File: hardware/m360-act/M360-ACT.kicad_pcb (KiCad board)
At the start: 2 copper layers, 100 x 80 mm, 30 parts, among them J1 5V do quadro, J2 M360-RF, J3 RJ45 RELES-A, J4 RJ45 RELES-B, J5 RJ45 SENSORES, SW1 Repareamento, U1 AMS1117-3.3, U2 74HCT244, U3 CD74HC4067, U4 SRV05-4, U5 SRV05-4, U6 SRV05-4, U7 SRV05-4, U8 SRV05-4

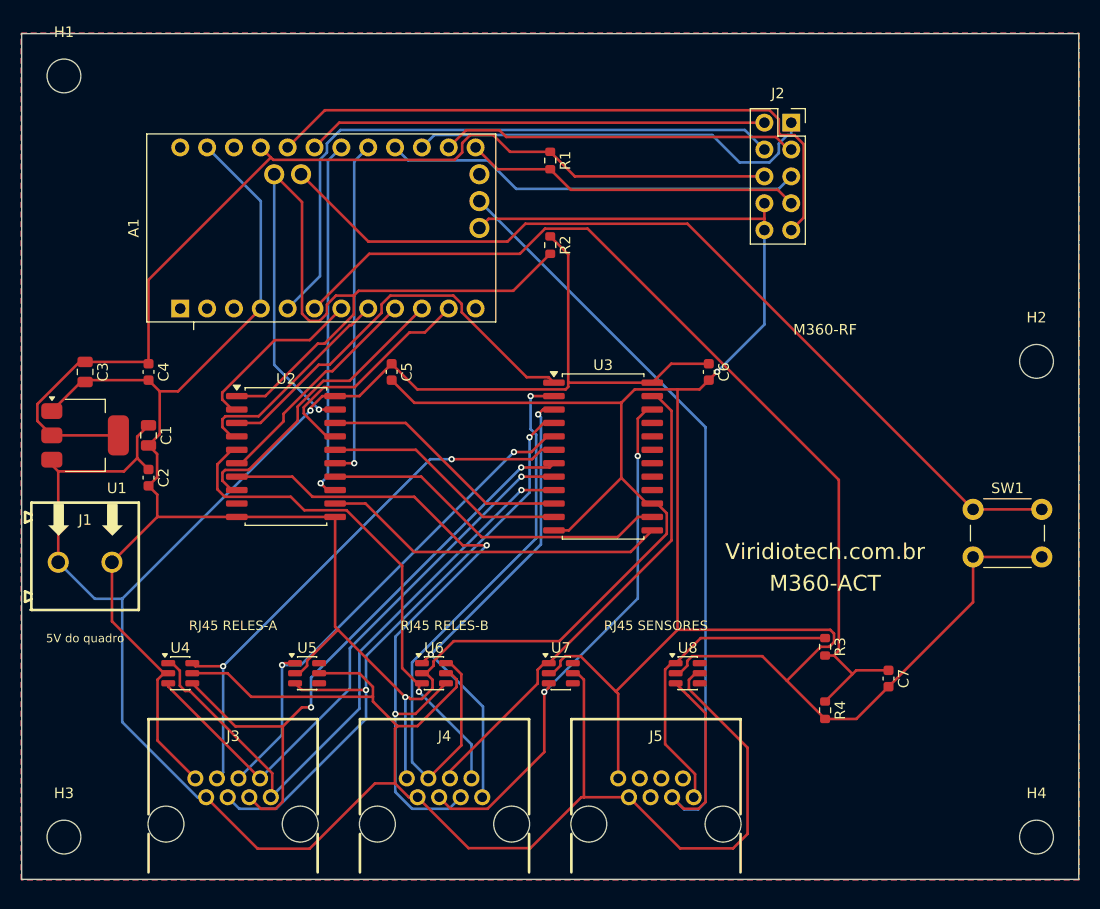
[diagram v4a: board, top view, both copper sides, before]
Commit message: feat(hardware): placa da M360-ACT refeita e arquivos de fabricação
- sincronizada com o esquemático (35 peças novas; U1 ME6211, SW1 reed)
- place_act.py reescrito: par de TVS a 180° atrás de cada RJ45, 100 ohm na
  ordem de saída dos TVS, U3 com I0-I7 para os TVS, reed na borda direita,
  fiduciais, área sem trilha em B.Cu sob os RJ45; borne J1 a rot 90 (entrada
  dos fios para a borda, datasheet C8465) e modelo 3D do borne corrigido
- roteamento pela §11.8: 15 pernas RJ45 -> TVS numa passada, em F.Cu;
  REL_CH0/CH6 desenhados à mão; tronco de +5V em 0,5 mm; classe Power
- ordem_tvs.py: contato por distância entre segmentos (pega X e sobreposição)
- silk_refs.py: referências posicionadas automaticamente
- correções da revisão adversarial da placa; reed: porta do quadro aberta
- fabricacao/: Gerbers, BOM e posição (53 peças, todas com LCSC)

DRC --severity-all 0/0, paridade idêntica, ordem_tvs act 15/15.

Co-Authored-By: Claude Opus 5 (1M context) <noreply@anthropic.com>
Claude-Session: https://claude.ai/code/session_012t7RkcrXvvpDVjKVimNu18
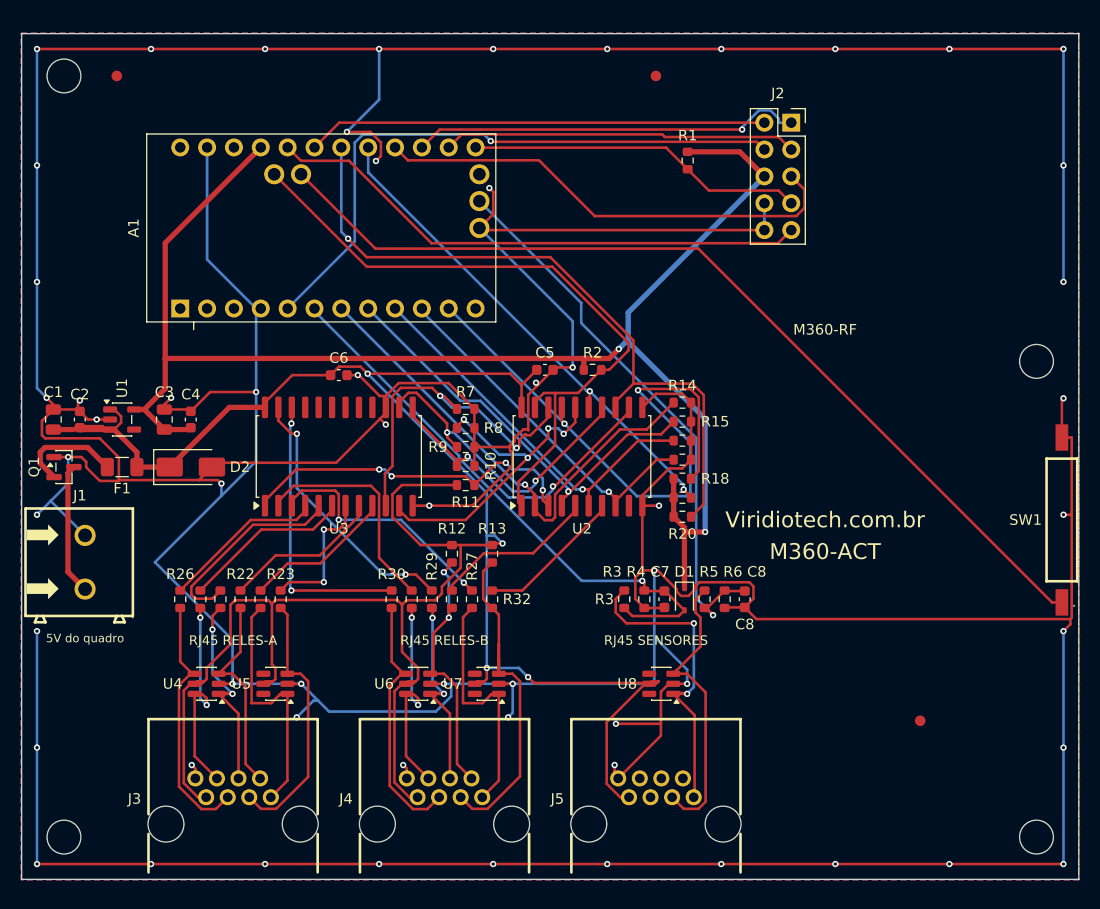
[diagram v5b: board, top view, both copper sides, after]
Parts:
- added C8: 100nF, Capacitor_SMD:C_0603_1608Metric, F.Cu at (168.4, 153.5)
- added D1: BAT54WS, Diode_SMD:D_SOD-323, F.Cu at (162.7, 153.5)
- added D2: SMAJ5.0A, Diode_SMD:D_SMA, F.Cu at (116.0, 141.0)
- added F1: 500mA, Fuse:Fuse_1206_3216Metric, F.Cu at (109.5, 141.0)
- added FID1: Fiducial_1mm_Mask2mm, Fiducial_1mm_Mask2mm, F.Cu at (109.0, 104.0)
- added FID2: Fiducial_1mm_Mask2mm, Fiducial_1mm_Mask2mm, F.Cu at (160.0, 104.0)
- added FID3: Fiducial_1mm_Mask2mm, Fiducial_1mm_Mask2mm, F.Cu at (185.0, 165.0)
- added Q1: AO3401A, Package_TO_SOT_SMD:SOT-23, F.Cu at (104.0, 141.0)
- added R10: 100k, Resistor_SMD:R_0603_1608Metric, F.Cu at (142.0, 140.9)
- added R11: 100k, Resistor_SMD:R_0603_1608Metric, F.Cu at (142.0, 142.7)
- added R12: 100k, Resistor_SMD:R_0603_1608Metric, F.Cu at (140.7, 149.2)
- added R13: 100k, Resistor_SMD:R_0603_1608Metric, F.Cu at (144.5, 149.2)
- added R14: 100k, Resistor_SMD:R_0603_1608Metric, F.Cu at (162.5, 134.9)
- added R15: 100k, Resistor_SMD:R_0603_1608Metric, F.Cu at (162.5, 136.7)
- added R16: 100k, Resistor_SMD:R_0603_1608Metric, F.Cu at (162.5, 138.5)
- added R17: 100k, Resistor_SMD:R_0603_1608Metric, F.Cu at (162.5, 140.3)
- added R18: 100k, Resistor_SMD:R_0603_1608Metric, F.Cu at (162.5, 142.1)
- added R19: 100k, Resistor_SMD:R_0603_1608Metric, F.Cu at (162.5, 143.9)
- added R20: 100k, Resistor_SMD:R_0603_1608Metric, F.Cu at (162.5, 145.7)
- added R21: 100, Resistor_SMD:R_0603_1608Metric, F.Cu at (122.6, 153.5)
- added R22: 100, Resistor_SMD:R_0603_1608Metric, F.Cu at (120.7, 153.5)
- added R23: 100, Resistor_SMD:R_0603_1608Metric, F.Cu at (124.5, 153.5)
- added R24: 100, Resistor_SMD:R_0603_1608Metric, F.Cu at (116.9, 153.5)
- added R25: 100, Resistor_SMD:R_0603_1608Metric, F.Cu at (118.8, 153.5)
- added R26: 100, Resistor_SMD:R_0603_1608Metric, F.Cu at (115.0, 153.5)
- added R27: 100, Resistor_SMD:R_0603_1608Metric, F.Cu at (142.6, 153.5)
- added R28: 100, Resistor_SMD:R_0603_1608Metric, F.Cu at (136.9, 153.5)
- added R29: 100, Resistor_SMD:R_0603_1608Metric, F.Cu at (138.8, 153.5)
- added R30: 100, Resistor_SMD:R_0603_1608Metric, F.Cu at (135.0, 153.5)
- added R31: 100, Resistor_SMD:R_0603_1608Metric, F.Cu at (140.7, 153.5)
- added R32: 100, Resistor_SMD:R_0603_1608Metric, F.Cu at (144.5, 153.5)
- added R5: 10k, Resistor_SMD:R_0603_1608Metric, F.Cu at (164.6, 153.5)
- added R6: 20k, Resistor_SMD:R_0603_1608Metric, F.Cu at (166.5, 153.5)
- added R7: 100k, Resistor_SMD:R_0603_1608Metric, F.Cu at (142.0, 135.5)
- added R8: 100k, Resistor_SMD:R_0603_1608Metric, F.Cu at (142.0, 137.3)
- added R9: 100k, Resistor_SMD:R_0603_1608Metric, F.Cu at (142.0, 139.1)
- SW1: value Repareamento -> Reed; footprint Button_Switch_THT:SW_PUSH_6mm -> M360:Reed_Littelfuse_59170
- U1: value AMS1117-3.3 -> ME6211C33M5; footprint Package_TO_SOT_SMD:SOT-223-3_TabPin2 -> Package_TO_SOT_SMD:SOT-23-5
- moved C6 35.0 mm to (130.0, 132.3), turned to 0 degrees
- moved U2 28.0 mm to (153.0, 140.0), turned to 90 degrees
- moved U3 25.0 mm to (130.0, 140.0), turned to 90 degrees
- moved C7 22.5 mm to (160.8, 153.5)
- moved R4 20.1 mm to (158.9, 153.5)
- moved R3 19.5 mm to (157.0, 153.5)
- moved C5 14.5 mm to (149.5, 131.8), turned to 0 degrees
- moved R1 13.0 mm to (163.0, 112.0)
- moved R2 12.5 mm to (154.0, 131.8), turned to 0 degrees
- moved C1 9.12 mm to (103.0, 136.5), turned to 90 degrees
- moved C3 8.75 mm to (113.5, 136.5), turned to 90 degrees
- moved C2 8.51 mm to (105.5, 136.5), turned to 90 degrees
- moved SW1 8.46 mm to (198.4, 146.0), turned to 90 degrees
- moved U7 7.07 mm to (144.0, 161.5), turned to 180 degrees
- moved C4 6.02 mm to (116.0, 136.5), turned to 90 degrees
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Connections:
- J1 pad 1: +5V -> VIN_RAW
- J5 pad 3: AUX_A6 -> AUX_A6_IN
- R2 pad 1: +5V -> 3V3
- U1 pad 1: GND -> +5V
- U1 pad 2: 3V3 -> GND
- U2 pad 5: REL_NFT -> REL_NFT_BUF
- U2 pad 7: REL_OXI -> REL_OXI_BUF
- U3 pad 2: REL_CH7 -> REL_CH7_MUX
- U3 pad 22: REL_CH9 -> REL_CH9_MUX
- U3 pad 23: REL_CH8 -> REL_CH8_MUX
- U3 pad 3: REL_CH6 -> REL_CH6_MUX
- U3 pad 4: REL_CH5 -> REL_CH5_MUX
- U3 pad 5: REL_CH4 -> REL_CH4_MUX
- U3 pad 6: REL_CH3 -> REL_CH3_MUX
- U3 pad 7: REL_CH2 -> REL_CH2_MUX
- U3 pad 8: REL_CH1 -> REL_CH1_MUX
- U3 pad 9: REL_CH0 -> REL_CH0_MUX
- U4 pad 1: REL_CH0 -> REL_CH4
- U4 pad 4: REL_CH2 -> REL_CH5
- U5 pad 1: REL_CH4 -> REL_CH0
- U5 pad 3: REL_CH5 -> REL_CH2
- U6 pad 1: REL_CH6 -> REL_CH8
- U6 pad 4: REL_OXI -> REL_CH9
- U7 pad 1: REL_CH8 -> REL_CH6
- U7 pad 3: REL_CH9 -> REL_OXI
- U8 pad 3: AUX_A6 -> AUX_A6_IN
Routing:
- net GND: track 387.8 -> 747.5 mm, vias 2 -> 59
- net 3V3: track 97.6 -> 145.2 mm, vias 0 -> 2
- net +5V: track 271.0 -> 230.6 mm, vias 1 -> 4
- net REL_CH7: track 57.1 -> 19.6 mm, vias 1 -> 2
- net REL_CH0: track 59.3 -> 22.8 mm, vias 1 -> 0
- net FLOW_DIV: track 89.9 -> 53.8 mm, vias 0 -> 1
- net MUX_SIG_3V3: track 22.0 -> 57.8 mm, vias 0 -> 2
- net REL_CH5: track 59.9 -> 24.2 mm, vias 2 -> 0
- net REL_CH1: track 54.5 -> 19.7 mm, vias 1 -> 0
- net REL_CH3: track 53.7 -> 19.6 mm
- net REL_CH2: track 58.9 -> 25.4 mm, vias 2 -> 0
- net AUX_A6: track 85.9 -> 53.7 mm, vias 0 -> 1
- net REL_OXI: track 66.5 -> 34.6 mm, vias 2 -> 0
- net OXI_3V3: track 34.2 -> 66.0 mm
- net MUX_S0_3V3: track 17.0 -> 46.5 mm, vias 0 -> 1
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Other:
- board text added: "R3 R4 C7 D1 R5 R6 C8"

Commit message: fix(hardware): ACT — placa de 93 mm e roteamento completado após ajustes do usuário
- ajustes do usuário: borda direita em x 193, soquete J2 a 90°, SW1, H2 e H4
  reposicionados, marca e legenda do J2 em pé; place_act.py e silk_act.py
  passam a reproduzi-los
- contorno fechado em 93 x 80 mm; zonas de GND estendidas até a nova borda
  (por texto); SPI, DIO, RF_RESET, REED e trechos de GND/3V3 rerroteados com
  o resto travado; costura do perímetro refeita
- §11.7: SetOutline de zona pelo SWIG + SaveBoard zerou o .kicad_pcb
- fabricacao/ regenerado (53 peças)

DRC --severity-all 0/0, paridade idêntica, ordem_tvs act 15/15.

Co-Authored-By: Claude Opus 5 (1M context) <noreply@anthropic.com>
Claude-Session: https://claude.ai/code/session_012t7RkcrXvvpDVjKVimNu18
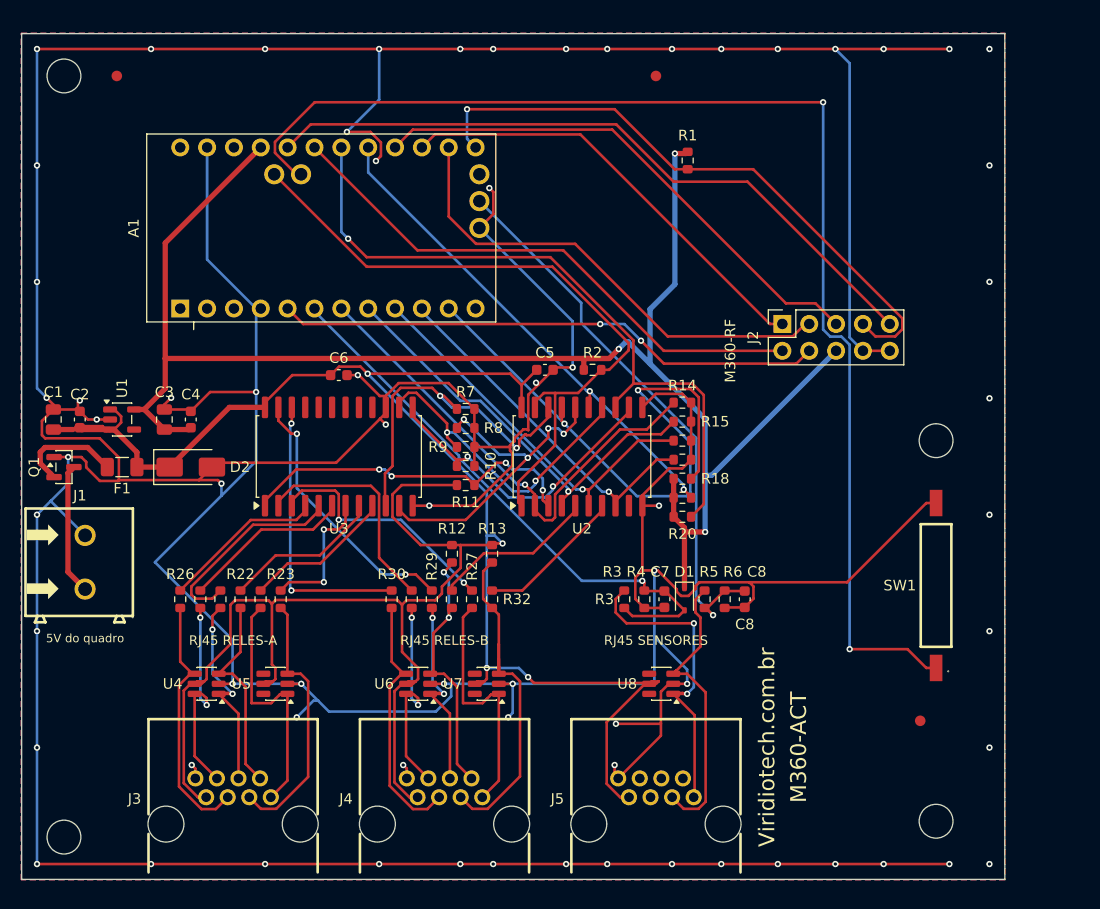
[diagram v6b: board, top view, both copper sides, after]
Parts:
- moved J2 19.1 mm to (172.0, 127.5), turned to 90 degrees
- moved SW1 13.4 mm to (186.5, 152.2)
- moved H2 12.1 mm to (186.5, 138.5)
- moved H4 9.62 mm to (186.5, 174.5)
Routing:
- net GND: track 747.5 -> 661.1 mm, vias 59 -> 69
- net REED: track 88.7 -> 120.1 mm, vias 0 -> 2
- net NSS: track 32.0 -> 58.8 mm, vias 0 -> 1
- net RF_RESET: track 51.9 -> 65.7 mm
- net MOSI: track 33.5 -> 45.8 mm
- net 3V3: track 145.2 -> 155.4 mm, vias 2 -> 3
- net DIO1: track 43.5 -> 52.2 mm
- net DIO0: track 58.0 -> 52.0 mm, vias 1 -> 2
- net MISO: track 37.2 -> 42.0 mm, vias 1 -> 0
- net SCK: track 45.2 -> 50.0 mm
- net REL_OXI: track 34.6 -> 35.3 mm
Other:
- board size 100 x 80 mm -> 93 x 80 mm

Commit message: feat(hardware): header 1x8 do nRF24 legado nas placas GW, LP e ACT
- esquemáticos: header 1x8 "nRF24 legado" (GW J4, LP J5, ACT J6; C492407,
  solda manual, fora do BOM e da posição) e 10 uF 0805 (C5/C16/C9, C15850)
  nas mesmas redes do soquete do mezanino: CE = DIO0, CSN = NSS, IRQ = DIO1
  (sem ligação na GW). Um rádio por placa: nRF24 OU mezanino RFM95W
- tools/add_nrf_header.py: grava símbolo, fios e labels por texto, embute o
  Conn_01x08 stock e confere colisão; netdiff só nas redes previstas, ERC 0,
  campos e lib_symbols inalterados nas três folhas
- placas rerroteadas sem apagar a fiação existente (DSN com fios fixos e
  cobertos por área proibida, mais áreas proibidas sobre os fiduciais);
  vias de GND junto do pino 8 e do capacitor; legenda "nRF24 OU mezanino"
  e "CE" no pino 1. GW 287 trilhas/43 vias, LP 855/135, ACT 939/141;
  DRC --severity-all 0/0, paridade idêntica, ordem_tvs 13/13 e 15/15
- fabricacao/ regerada: GW 15, LP 53, ACT 54 peças
- ARQUITETURA §2 (decisão 15), §4.2, §5.2, §6.1, §8, §9, §9.1; datasheet
  C492407 em docs/datasheets. Firmware pendente: MY_RF24_CE_PIN=5 (GW) e
  =2 (LP/ACT), a testar na bancada

Co-Authored-By: Claude Fable 5.1 <noreply@anthropic.com>
Claude-Session: https://claude.ai/code/session_01M8U92DFNnZt7SqLtzrKYSR
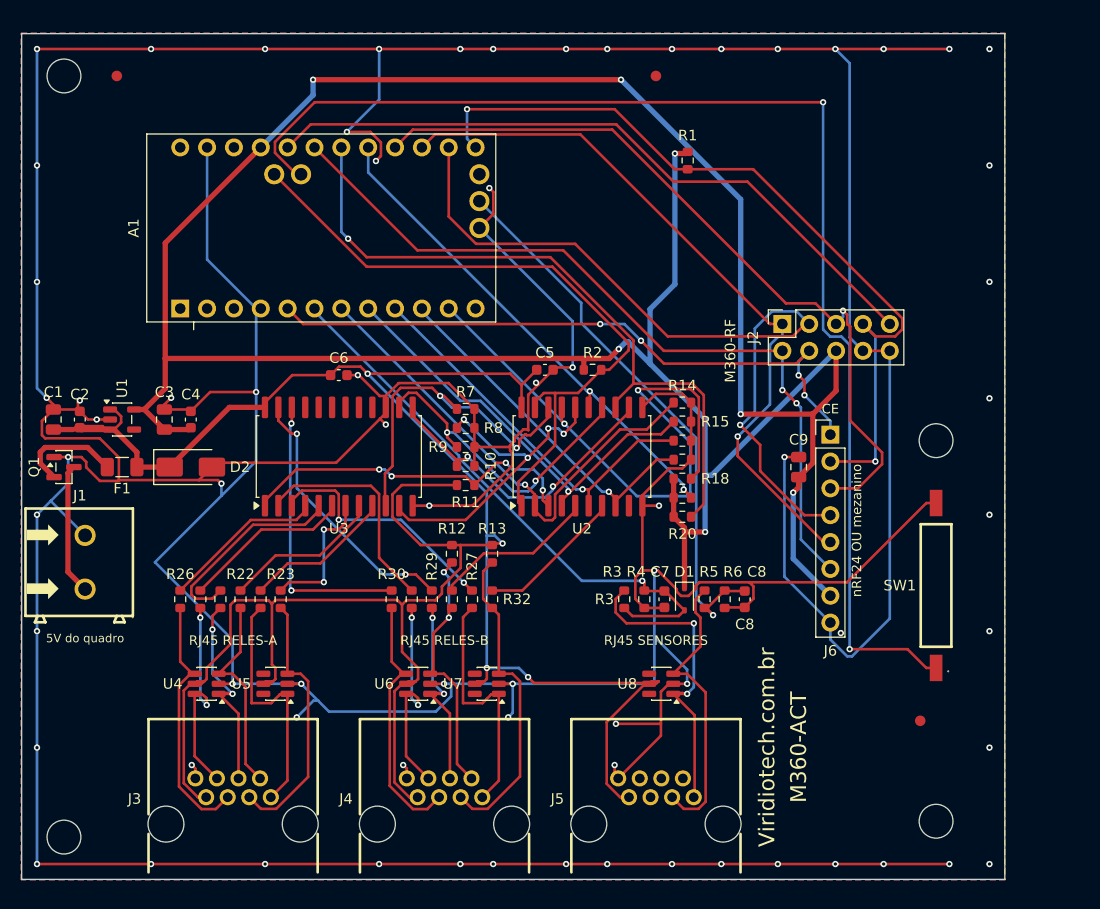
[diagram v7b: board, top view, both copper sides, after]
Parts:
- added C9: 10uF, Capacitor_SMD:C_0805_2012Metric, F.Cu at (173.5, 141.0)
- added J6: nRF24 legado, Connector_PinHeader_2.54mm:PinHeader_1x08_P2.54mm_Vertical, F.Cu at (176.5, 137.9)
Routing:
- net 3V3: track 155.4 -> 262.5 mm, vias 3 -> 7
- net GND: track 661.1 -> 714.6 mm, vias 69 -> 71
- net MOSI: track 45.8 -> 75.4 mm, vias 0 -> 1
- net MISO: track 42.0 -> 68.7 mm, vias 0 -> 1
- net SCK: track 50.0 -> 73.5 mm, vias 0 -> 1
- net DIO1: track 52.2 -> 74.8 mm, vias 0 -> 2
- net NSS: track 58.8 -> 76.6 mm, vias 1 -> 2
- net DIO0: track 52.0 -> 61.6 mm, vias 2 -> 4
- net REL_OXI: track 35.3 -> 30.4 mm
- net AUX_A6_IN: track 28.7 -> 27.8 mm
- net VIN_RAW: track 12.8 -> 12.0 mm
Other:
- board text added: "CE"
- board text added: "nRF24 OU mezanino"
